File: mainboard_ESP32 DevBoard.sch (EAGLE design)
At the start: 43 parts, among them IC1 OP-AMP-2-LONG, IC2 OP-AMP-2-LONG, IC3 74HC08N, K1 AQH213, X1 JST-XH-02-PIN-LONG-PAD, X2 JST-XH-04-PIN-LONG-PAD, X3 1751248, X4 1751248, X5 JST-XH-04-PIN-LONG-PAD

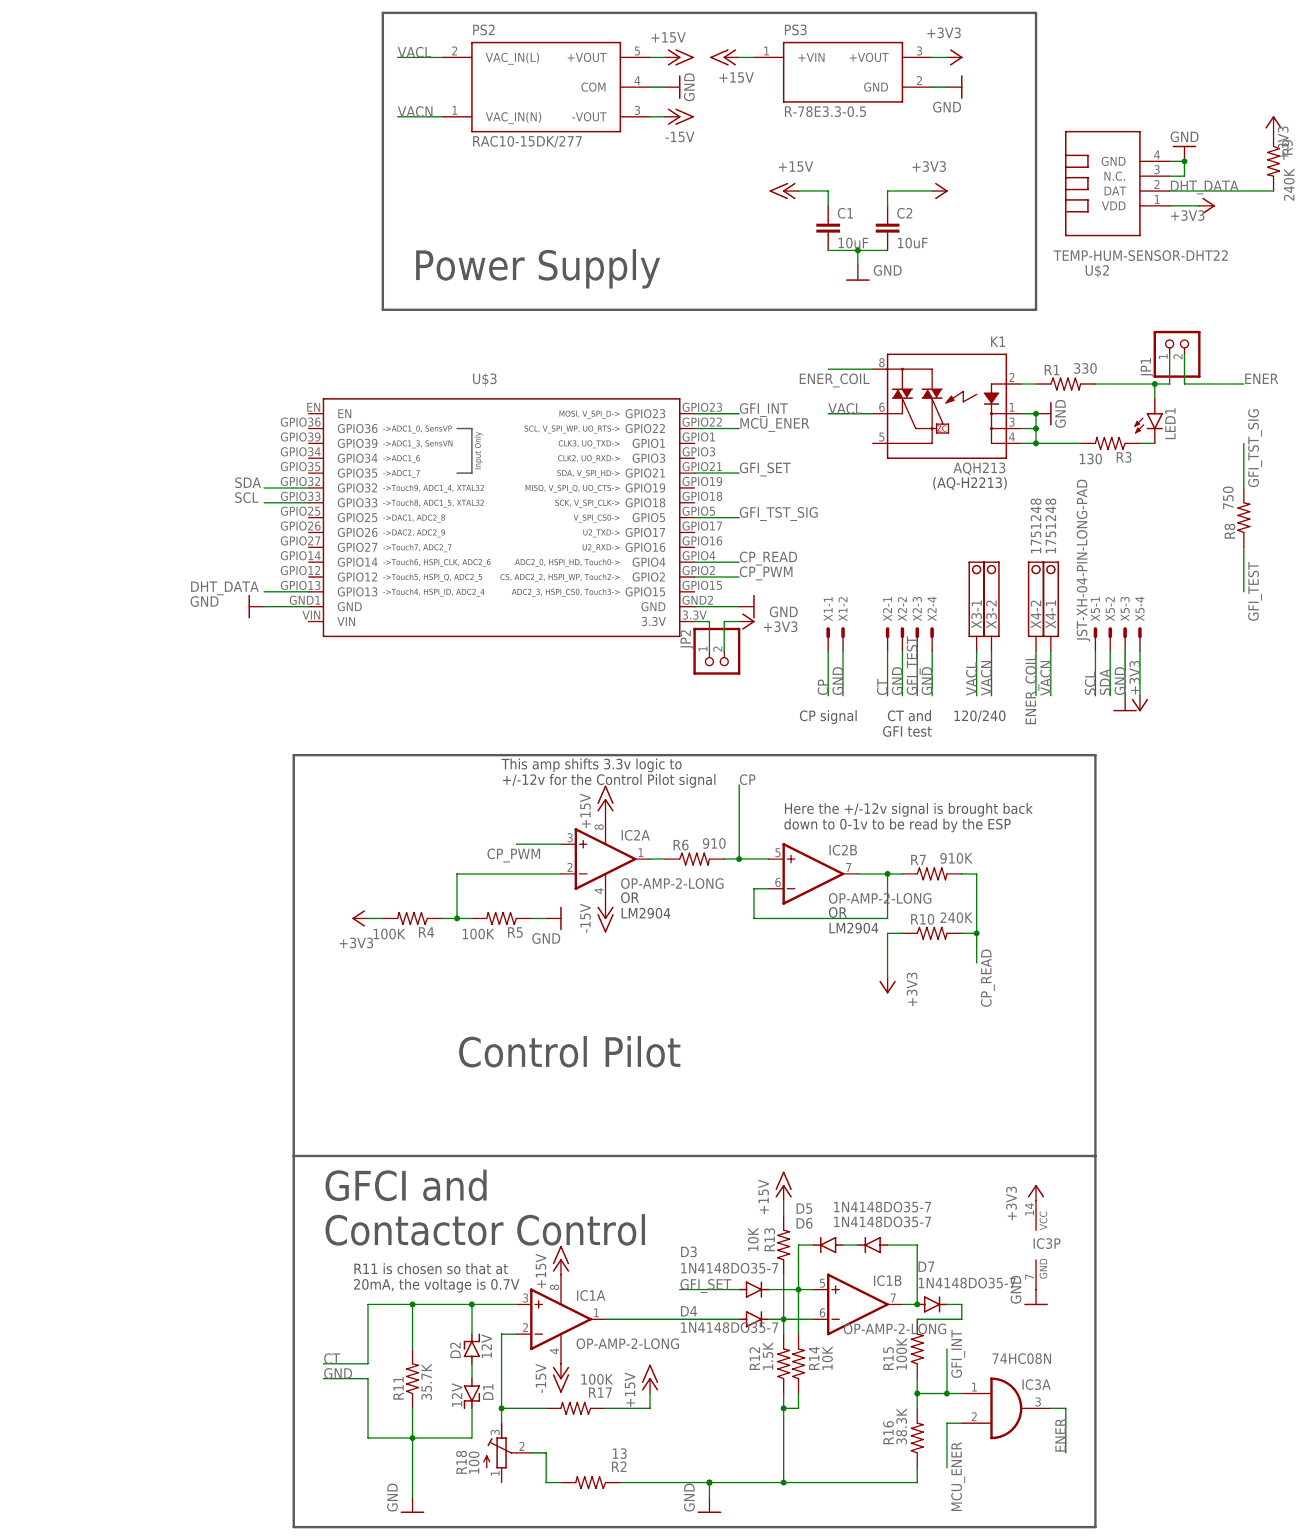
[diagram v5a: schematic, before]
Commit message: Made board single-sided friendly (P2P wiring needed). Tweaked some more resistor values. Added missing resistor to CP read level shifter
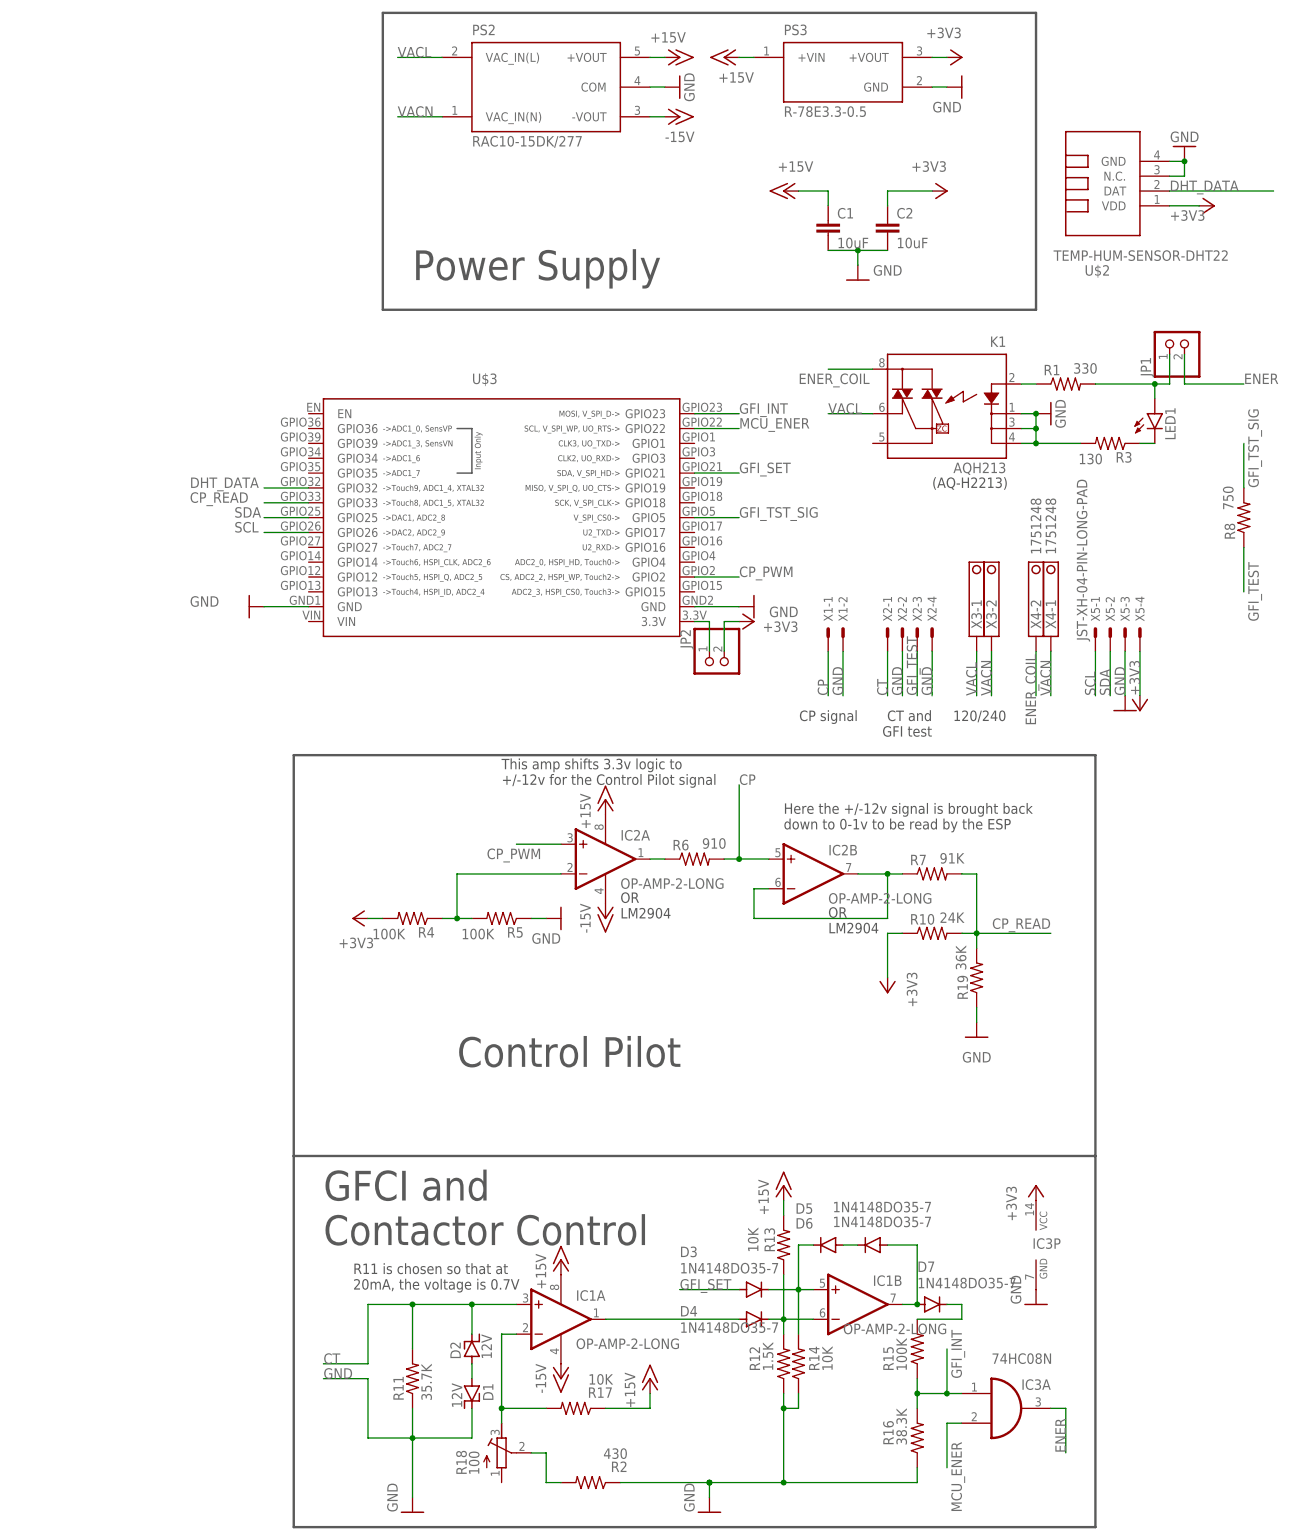
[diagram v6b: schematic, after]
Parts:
- removed R9: 240K, Passive:RESISTORL
- added R19: 36K, Passive:RESISTORL
- R10: value 240K -> 24K
- R17: value 100K -> 10K
- R18: device rcl:R-TRIMM64W -> rcl:R-TRIMM3296W
- R2: value 13 -> 430
- R7: value 910K -> 91K
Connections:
- net +3V3: no longer R9.1
- net CP_READ: now also R19.2, U$3.GPIO33; no longer U$3.GPIO4
- net DHT_DATA: now also U$3.GPIO32; no longer R9.2, U$3.GPIO13
- net GND: now also R19.1
- net SCL: now also U$3.GPIO26; no longer U$3.GPIO33
- net SDA: now also U$3.GPIO25; no longer U$3.GPIO32
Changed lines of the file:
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@@
 <part name="GND8" library="supply1" library_urn="urn:adsk.eagle:library:371" deviceset="GND" device=""/>
 <part name="R6" library="Passive" deviceset="RESISTOR" device="L" value="910"/>
-<part name="R7" library="Passive" deviceset="RESISTOR" device="L" value="910K"/>
-<part name="R10" library="Passive" deviceset="RESISTOR" device="L" value="240K"/>
+<part name="R7" library="Passive" deviceset="RESISTOR" device="L" value="91K"/>
+<part name="R10" library="Passive" deviceset="RESISTOR" device="L" value="24K"/>
 <part name="+3V6" library="supply1" library_urn="urn:adsk.eagle:library:371" deviceset="+3V3" device=""/>
 <part name="+3V3" library="supply1" library_urn="urn:adsk.eagle:library:371" deviceset="+3V3" device=""/>
@@
 <part name="GND14" library="supply1" library_urn="urn:adsk.eagle:library:371" deviceset="GND" device=""/>
 <part name="+3V7" library="supply1" library_urn="urn:adsk.eagle:library:371" deviceset="+3V3" device=""/>
-<part name="R17" library="Passive" deviceset="RESISTOR" device="L" value="100K"/>
+<part name="R17" library="Passive" deviceset="RESISTOR" device="L" value="10K"/>
 <part name="GND15" library="supply1" library_urn="urn:adsk.eagle:library:371" deviceset="GND" device=""/>
-<part name="R18" library="rcl" library_urn="urn:adsk.eagle:library:334" deviceset="R-TRIMM" device="64W" package3d_urn="urn:adsk.eagle:package:23748/1" value="100"/>
+<part name="R18" library="rcl" library_urn="urn:adsk.eagle:library:334" deviceset="R-TRIMM" device="3296W" package3d_urn="urn:adsk.eagle:package:26033/1" value="100"/>
 <part name="X1" library="Rembrandt Electronics - JST XH Connectors v1-0" deviceset="JST-XH-02-PIN" device="-LONG-PAD"/>
 <part name="X2" library="Rembrandt Electronics - JST XH Connectors v1-0" deviceset="JST-XH-04-PIN" device="-LONG-PAD"/>
 <part name="X3" library="con-phoenix-350" library_urn="urn:adsk.eagle:library:174" deviceset="1751248" device="" package3d_urn="urn:adsk.eagle:package:9395/1"/>
 <part name="X4" library="con-phoenix-350" library_urn="urn:adsk.eagle:library:174" deviceset="1751248" device="" package3d_urn="urn:adsk.eagle:package:9395/1"/>
-<part name="R2" library="Passive" deviceset="RESISTOR" device="L" value="13"/>
+<part name="R2" library="Passive" deviceset="RESISTOR" device="L" value="430"/>
 <part name="GND3" library="supply1" library_urn="urn:adsk.eagle:library:371" deviceset="GND" device=""/>
 <part name="U$3" library="ESP32" deviceset="ESP32-DOIT-V1" device=""/>
@@
 <part name="GND7" library="supply1" library_urn="urn:adsk.eagle:library:371" deviceset="GND" device=""/>
 <part name="+3V1" library="supply1" library_urn="urn:adsk.eagle:library:371" deviceset="+3V3" device=""/>
-<part name="R9" library="Passive" deviceset="RESISTOR" device="L" value="240K"/>
-<part name="+3V9" library="supply1" library_urn="urn:adsk.eagle:library:371" deviceset="+3V3" device=""/>
+<part name="R19" library="Passive" deviceset="RESISTOR" device="L" value="36K"/>
+<part name="GND9" library="supply1" library_urn="urn:adsk.eagle:library:371" deviceset="GND" device=""/>
 </parts>
 <sheets>
@@
 <attribute name="VALUE" x="137.16" y="35.56" size="1.778" layer="96" rot="R90"/>
 </instance>
-<instance part="R9" gate="G$1" x="160.02" y="127" smashed="yes" rot="R270">
-<attribute name="NAME" x="161.5186" y="130.81" size="1.778" layer="95" rot="R270"/>
-<attribute name="VALUE" x="161.798" y="125.73" size="1.778" layer="96" rot="R270"/>
-</instance>
-<instance part="+3V9" gate="G$1" x="160.02" y="134.62" smashed="yes">
-<attribute name="VALUE" x="162.56" y="127" size="1.778" layer="96" rot="R90"/>
+<instance part="R19" gate="G$1" x="109.22" y="-12.7" smashed="yes" rot="R90">
+<attribute name="NAME" x="107.7214" y="-16.51" size="1.778" layer="95" rot="R90"/>
+<attribute name="VALUE" x="107.442" y="-11.43" size="1.778" layer="96" rot="R90"/>
+</instance>
+<instance part="GND9" gate="1" x="109.22" y="-22.86" smashed="yes">
+<attribute name="VALUE" x="111.76" y="-25.4" size="1.778" layer="96" rot="R180"/>
 </instance>
 </instances>
@@
 <pinref part="GND7" gate="1" pin="GND"/>
 </segment>
+<segment>
+<pinref part="GND9" gate="1" pin="GND"/>
+<pinref part="R19" gate="G$1" pin="1"/>
+<wire x1="109.22" y1="-20.32" x2="109.22" y2="-17.78" width="0.1524" layer="91"/>
+</segment>
 </net>
 <net name="+3V3" class="0">
@@
 <wire x1="137.16" y1="43.18" x2="137.16" y2="35.56" width="0.1524" layer="91"/>
 <pinref part="+3V1" gate="G$1" pin="+3V3"/>
-</segment>
-<segment>
-<pinref part="R9" gate="G$1" pin="1"/>
-<pinref part="+3V9" gate="G$1" pin="+3V3"/>
 </segment>
 </net>
@@
 <wire x1="109.22" y1="5.08" x2="109.22" y2="-5.08" width="0.1524" layer="91"/>
 <pinref part="R10" gate="G$1" pin="2"/>
-<wire x1="109.22" y1="-5.08" x2="109.22" y2="-10.16" width="0.1524" layer="91"/>
 <wire x1="106.68" y1="-5.08" x2="109.22" y2="-5.08" width="0.1524" layer="91"/>
+<label x="121.92" y="-2.54" size="1.778" layer="95" rot="R180"/>
+<pinref part="R19" gate="G$1" pin="2"/>
+<wire x1="109.22" y1="-7.62" x2="109.22" y2="-5.08" width="0.1524" layer="91"/>
 <junction x="109.22" y="-5.08"/>
-<label x="111.76" y="-17.78" size="1.778" layer="95" rot="R90"/>
-</segment>
-<segment>
-<pinref part="U$3" gate="G$1" pin="GPIO4"/>
-<wire x1="60.96" y1="58.42" x2="68.58" y2="58.42" width="0.1524" layer="91"/>
-<label x="68.58" y="58.42" size="1.778" layer="95"/>
+<wire x1="109.22" y1="-5.08" x2="121.92" y2="-5.08" width="0.1524" layer="91"/>
+</segment>
+<segment>
+<pinref part="U$3" gate="G$1" pin="GPIO33"/>
+<wire x1="-5.08" y1="68.58" x2="-12.7" y2="68.58" width="0.1524" layer="91"/>
+<label x="-25.4" y="68.58" size="1.778" layer="95"/>
 </segment>
 </net>
@@
 <net name="DHT_DATA" class="0">
 <segment>
-<pinref part="U$3" gate="G$1" pin="GPIO13"/>
-<wire x1="-5.08" y1="53.34" x2="-12.7" y2="53.34" width="0.1524" layer="91"/>
-<label x="-25.4" y="53.34" size="1.778" layer="95"/>
-</segment>
-<segment>
 <pinref part="U$2" gate="G$1" pin="DAT"/>
 <label x="142.24" y="121.92" size="1.778" layer="95"/>
-<pinref part="R9" gate="G$1" pin="2"/>
 <wire x1="142.24" y1="121.92" x2="160.02" y2="121.92" width="0.1524" layer="91"/>
+</segment>
+<segment>
+<pinref part="U$3" gate="G$1" pin="GPIO32"/>
+<wire x1="-5.08" y1="71.12" x2="-12.7" y2="71.12" width="0.1524" layer="91"/>
+<label x="-25.4" y="71.12" size="1.778" layer="95"/>
 </segment>
 </net>
@@
 </segment>
 <segment>
-<pinref part="U$3" gate="G$1" pin="GPIO32"/>
-<wire x1="-5.08" y1="71.12" x2="-12.7" y2="71.12" width="0.1524" layer="91"/>
-<label x="-17.78" y="71.12" size="1.778" layer="95"/>
+<pinref part="U$3" gate="G$1" pin="GPIO25"/>
+<wire x1="-5.08" y1="66.04" x2="-12.7" y2="66.04" width="0.1524" layer="91"/>
+<label x="-17.78" y="66.04" size="1.778" layer="95"/>
 </segment>
 </net>
 <net name="SCL" class="0">
-<segment>
-<pinref part="U$3" gate="G$1" pin="GPIO33"/>
-<wire x1="-5.08" y1="68.58" x2="-12.7" y2="68.58" width="0.1524" layer="91"/>
-<label x="-17.78" y="68.58" size="1.778" layer="95"/>
-</segment>
 <segment>
 <pinref part="X5" gate="-1" pin="S"/>
@@
 <label x="129.54" y="35.56" size="1.778" layer="95" rot="R90"/>
 </segment>
-</net>
+<segment>
+<pinref part="U$3" gate="G$1" pin="GPIO26"/>
+<wire x1="-5.08" y1="63.5" x2="-12.7" y2="63.5" width="0.1524" layer="91"/>
+<label x="-17.78" y="63.5" size="1.778" layer="95"/>
+</segment>
+</net>

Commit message: Switched to +-12v, tweaked some R values to fit new psu. Also swapped CP opamp for an r2r one
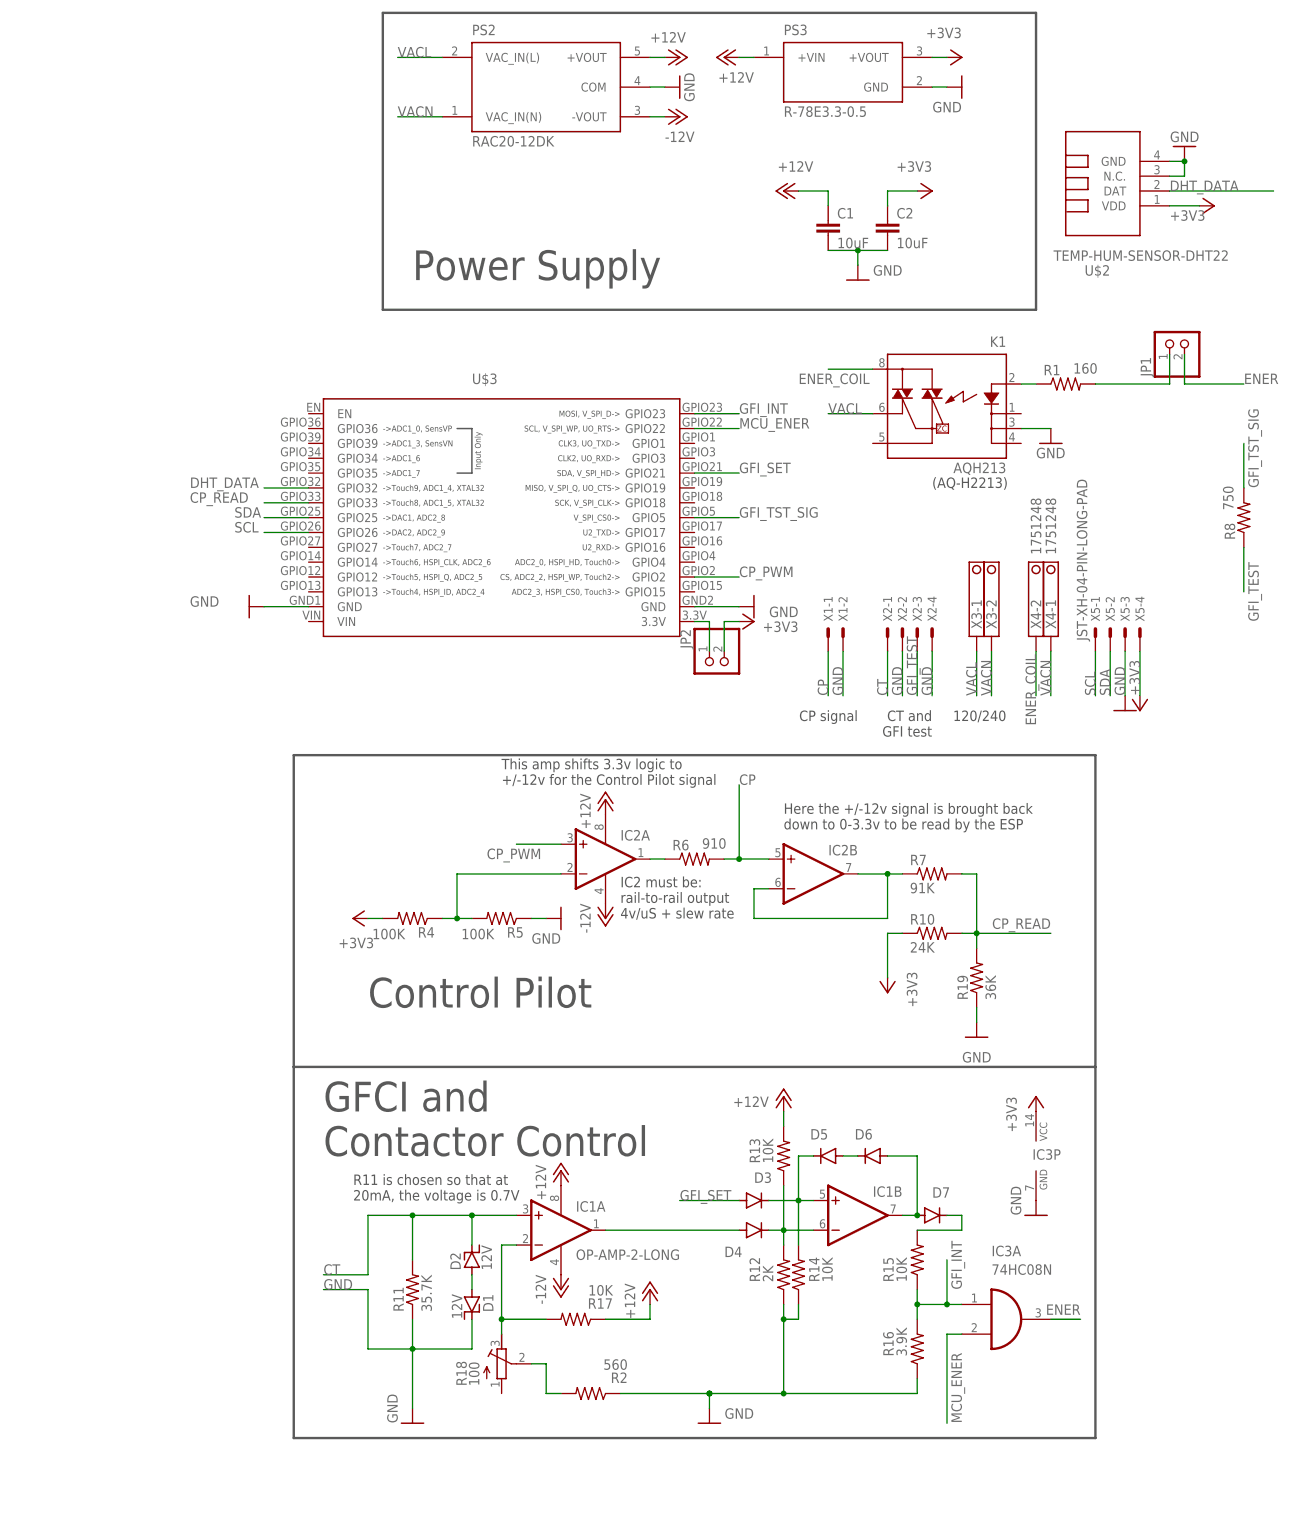
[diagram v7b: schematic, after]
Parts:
- removed LED1: (no value), led:LED3MM
- removed R3: 130, Passive:RESISTORL
- PS2: value RAC10-15DK/277 -> RAC20-12DK; device RAC10-15DK_277:RAC10-15DK/277 -> RAC20-12DK:RAC20-12DK
- R1: value 330 -> 160
- R12: value 1.5K -> 2K
- R15: value 100K -> 10K
- R16: value 38.3K -> 3.9K
- R2: value 430 -> 560
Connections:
- net +15V renamed +12V
- net -15V renamed -12V
- removed net N$8: LED1.C, R3.1
- net GND: no longer K1.K, K1.K2, R3.2
- net N$3: no longer LED1.A
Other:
- note added: "Here the +/-12v signal is brought back down to 0-3.3v to be read by the ESP"
- note added: "IC2 must be: rail-to-rail output 4v/uS + slew rate"
- note removed: "Here the +/-12v signal is brought back down to 0-1v to be read by the ESP"
- note removed: "OR LM2904"
- moved on the sheet: D1, D2, D3, D4, D5, D6, D7, IC1A, IC1B, IC3A, IC3P, R11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
